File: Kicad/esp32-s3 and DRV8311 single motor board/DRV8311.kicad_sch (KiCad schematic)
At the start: 11 parts, among them J3 Molex_PicoBlade_53048-0310 Ho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, U2 DRV8311HRRWR

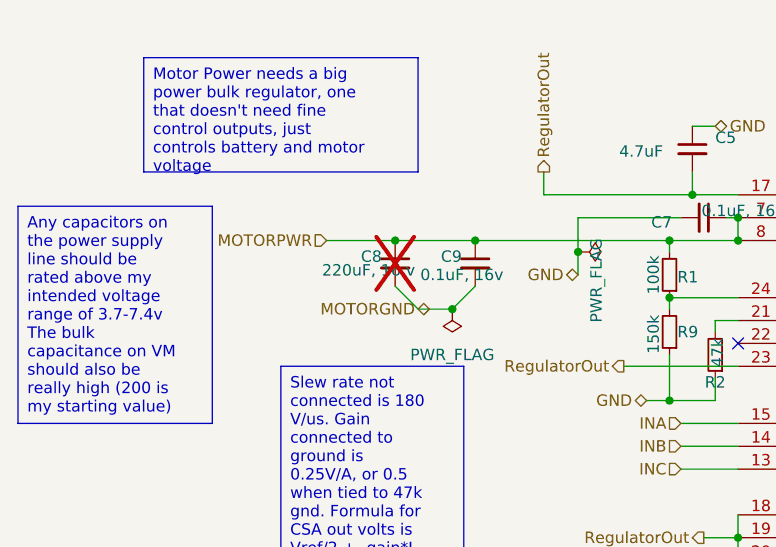
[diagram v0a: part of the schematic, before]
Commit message: Fixed Silkscreen
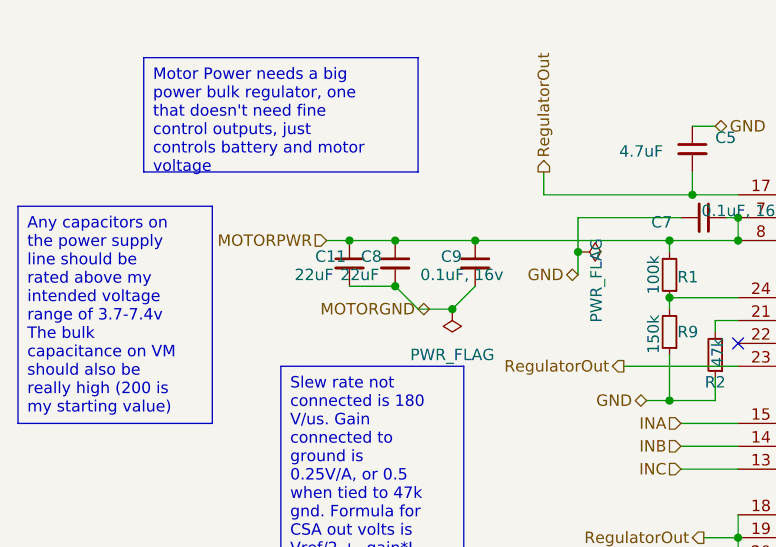
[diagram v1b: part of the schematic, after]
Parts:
- added C11: 22uF, Capacitor_SMD:C_0603_1608Metric_Pad1.08x0.95mm_HandSolder, symbol Device:C_Small
- C8: value 220uF, 16 v -> 22uF; footprint Capacitor_SMD:C_1206_3216Metric_Pad1.33x1.80mm_HandSolder -> Capacitor_SMD:C_0603_1608Metric_Pad1.08x0.95mm_HandSolder; now fitted; now in the parts list
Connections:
- net MOTORGND: now also C11.2
- net MOTORPWR: now also C11.1
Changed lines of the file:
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@@
+	)
+	(junction
+		(at 64.77 59.69)
+		(diameter 0)
+		(color 0 0 0 0)
+	)
+	(junction
+		(at 107.95 92.71)
+		(diameter 0)
+		(color 0 0 0 0)
+	)
+	(junction
+		(at 100.33 77.47)
+		(diameter 0)
+		(color 0 0 0 0)
+	)
+	(junction
+		(at 69.85 64.77)
+		(diameter 0)
+		(color 0 0 0 0)
+	)
+	(junction
+		(at 78.74 59.69)
+		(diameter 0)
+		(color 0 0 0 0)
+	)
+	(junction
+		(at 107.95 57.15)
+		(diameter 0)
+		(color 0 0 0 0)
+	)
+	(junction
+		(at 153.67 54.61)
+		(diameter 0)
+		(color 0 0 0 0)
 	)
 	(junction
@@
 		(color 0 0 0 0)
 	)
-	(junction
-		(at 107.95 92.71)
-		(diameter 0)
-		(color 0 0 0 0)
-	)
-	(junction
-		(at 100.33 77.47)
-		(diameter 0)
-		(color 0 0 0 0)
-	)
-	(junction
-		(at 78.74 59.69)
-		(diameter 0)
-		(color 0 0 0 0)
-	)
-	(junction
-		(at 107.95 57.15)
-		(diameter 0)
-		(color 0 0 0 0)
-	)
-	(junction
-		(at 153.67 54.61)
-		(diameter 0)
-		(color 0 0 0 0)
-	)
 	(no_connect
 		(at 107.95 71.12)
@@
 	(wire
 		(pts
+			(xy 64.77 64.77) (xy 69.85 64.77)
+		)
+		(stroke
+			(width 0)
+			(type default)
+		)
+	)
+	(wire
+		(pts
 			(xy 102.87 54.61) (xy 102.87 52.07)
 		)
@@
 	(wire
 		(pts
-			(xy 62.23 59.69) (xy 69.85 59.69)
-		)
-		(stroke
-			(width 0)
-			(type default)
-		)
-	)
-	(wire
-		(pts
 			(xy 86.36 54.61) (xy 102.87 54.61)
 		)
@@
 	(wire
 		(pts
+			(xy 64.77 59.69) (xy 69.85 59.69)
+		)
+		(stroke
+			(width 0)
+			(type default)
+		)
+	)
+	(wire
+		(pts
 			(xy 106.68 57.15) (xy 107.95 57.15)
 		)
@@
 	(wire
 		(pts
+			(xy 69.85 59.69) (xy 78.74 59.69)
+		)
+		(stroke
+			(width 0)
+			(type default)
+		)
+	)
+	(wire
+		(pts
 			(xy 152.4 102.87) (xy 161.29 102.87)
 		)
@@
 	(wire
 		(pts
-			(xy 69.85 59.69) (xy 78.74 59.69)
+			(xy 62.23 59.69) (xy 64.77 59.69)
 		)
 		(stroke
@@
 		(unit 1)
 		(exclude_from_sim no)
-		(in_bom no)
+		(in_bom yes)
 		(on_board yes)
-		(dnp yes)
+		(dnp no)
 		(property "Reference" "C8"
 			(at 66.04 61.468 0)
@@
 			)
 		)
-		(property "Value" "220uF, 16 v"
-			(at 61.722 62.992 0)
+		(property "Value" "22uF"
+			(at 63.754 63.5 0)
 			(effects
 				(font
@@
 			)
 		)
-		(property "Footprint" "Capacitor_SMD:C_1206_3216Metric_Pad1.33x1.80mm_HandSolder"
+		(property "Footprint" "Capacitor_SMD:C_0603_1608Metric_Pad1.08x0.95mm_HandSolder"
 			(at 69.85 62.23 0)
 			(effects
@@
 		)
 		(instances
-			(project "stm32g070 and DRV8311 single motor board - V1 Alpha"
+			(project "esp32-s3 and DRV8311 single motor board"
 				(path "/eb3f183d-8bb1-43a5-a363-092ed67891e3/5c02fed6-da20-4eef-a2eb-99e8043b232c"
 					(reference "C8")
@@
 					(unit 1)
 				)
+			)
+		)
+	)
+	(symbol
+		(lib_id "Device:C_Small")
+		(at 64.77 62.23 0)
+		(unit 1)
+		(exclude_from_sim no)
+		(in_bom yes)
+		(on_board yes)
+		(dnp no)
+		(property "Reference" "C11"
+			(at 60.96 61.468 0)
+			(effects
+				(font
+					(size 1.27 1.27)
+				)
+				(justify left)
+			)
+		)
+		(property "Value" "22uF"
+			(at 58.674 63.5 0)
+			(effects
+				(font
+					(size 1.27 1.27)
+				)
+				(justify left)
+			)
+		)
+		(property "Footprint" "Capacitor_SMD:C_0603_1608Metric_Pad1.08x0.95mm_HandSolder"
+			(at 64.77 62.23 0)
+			(effects
+				(font
+					(size 1.27 1.27)
+				)
+				(hide yes)
+			)
+		)
+		(property "Datasheet" "~"
+			(at 64.77 62.23 0)
+			(effects
+				(font
+					(size 1.27 1.27)
+				)
+				(hide yes)
+			)
+		)
+		(property "Description" "Unpolarized capacitor, small symbol"
+			(at 64.77 62.23 0)
+			(effects
+				(font
+					(size 1.27 1.27)
+				)
+				(hide yes)
+			)
+		)
+		(pin "1"
+		)
+		(pin "2"
+		)
+		(instances
+			(project "esp32-s3 and DRV8311 single motor board"
+				(path "/eb3f183d-8bb1-43a5-a363-092ed67891e3/5c02fed6-da20-4eef-a2eb-99e8043b232c"
+					(reference "C11")
+					(unit 1)
+				)
